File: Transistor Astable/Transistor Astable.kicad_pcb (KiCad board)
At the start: 2 copper layers, 12 parts, among them Q1 2N3904, Q2 2N3904

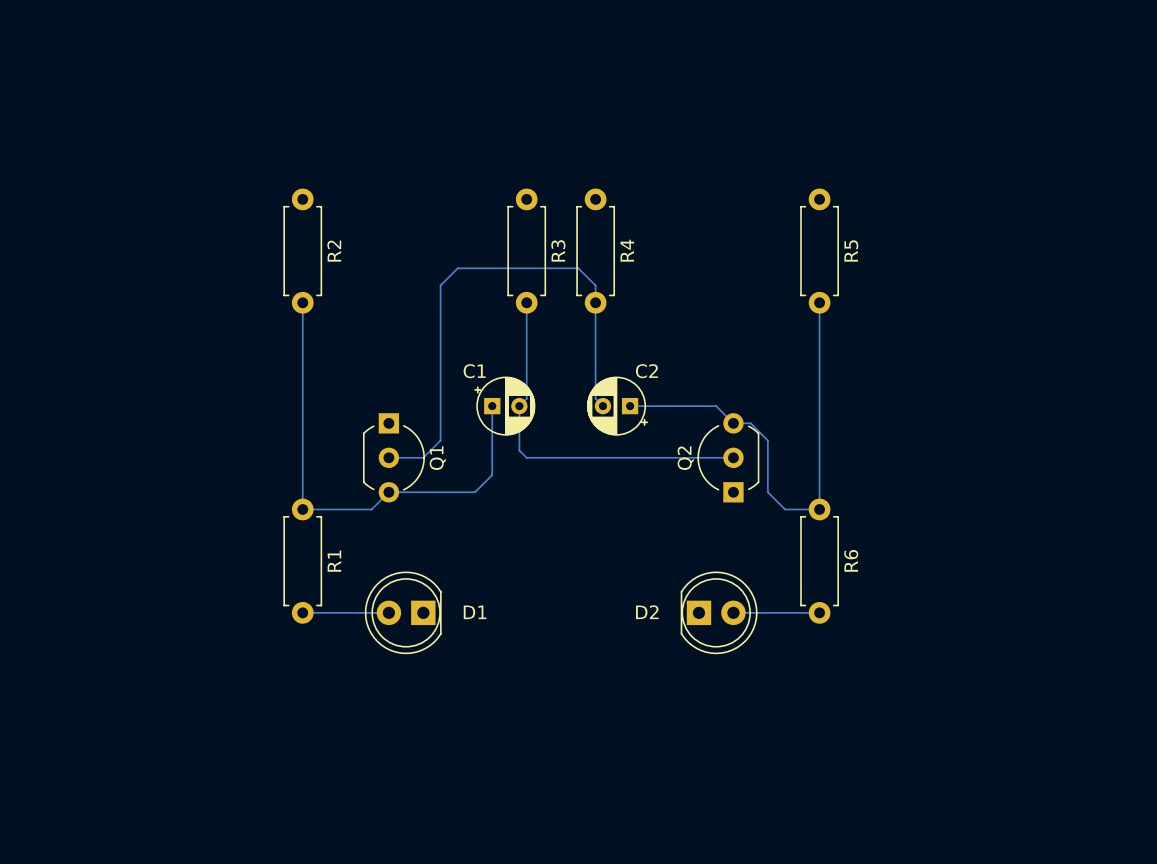
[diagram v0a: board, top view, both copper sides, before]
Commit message: Adding footprint and initial routing
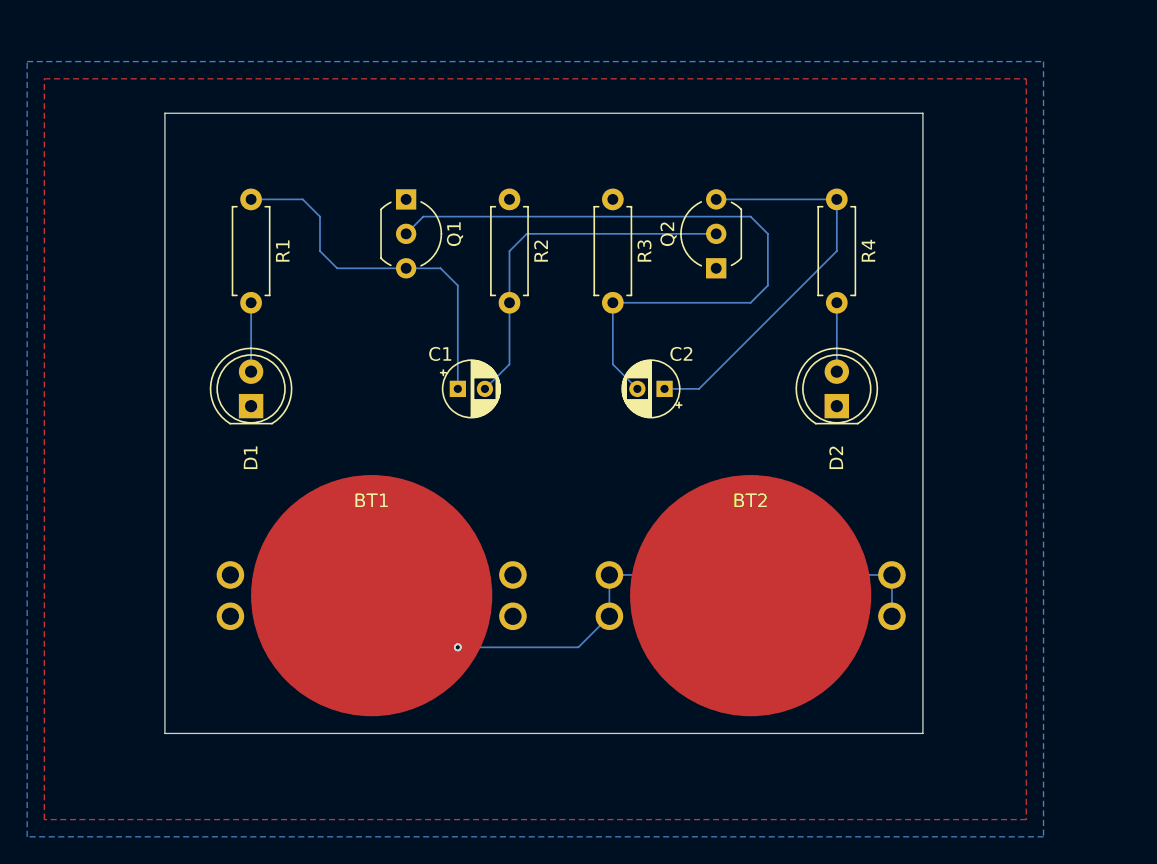
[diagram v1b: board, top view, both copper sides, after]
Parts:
- removed the R1 at (82.5, 95.2)
- removed R6: 470, Resistor_THT:R_Axial_DIN0207_L6.3mm_D2.5mm_P7.62mm_Horizontal
- added BT1: Battery_Cell, Transistor Astable:BattHold_Linx_CR2032, F.Cu at (87.6, 101.6)
- added BT2: Battery_Cell, Transistor Astable:BattHold_Linx_CR2032, F.Cu at (115.6, 101.6)
- Q1, Q2: value 2N3904 -> 2N3906
- R1: renamed from R2; value 680 -> 1k
- R4: renamed from R5; value 680 -> 1k
- moved D1 19.8 mm to (78.7, 87.6), turned to 90 degrees
- moved D2 18.3 mm to (121.9, 87.6), turned to 90 degrees
- moved Q1 16.6 mm to (90.2, 72.4)
- moved Q2 16.6 mm to (113.0, 77.5)
- moved R1 3.81 mm to (78.7, 72.4)
- moved C1 2.84 mm to (94.0, 86.4)
- moved C2 2.84 mm to (109.2, 86.4)
- moved R2 1.27 mm to (97.8, 72.4)
- moved R3 1.27 mm to (105.4, 72.4)
- moved R4 1.27 mm to (121.9, 72.4)
- renumbered R3 to R2, R4 to R3
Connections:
- Q1 pad 1: GND -> +6V
- Q2 pad 1: GND -> +6V
- R1 pad 1: +6V -> Net-(C1-Pad1)
- R1 pad 2: Net-(C1-Pad1) -> Net-(D1-Pad2)
- R2 pad 1: +6V -> GND
- R3 pad 1: +6V -> GND
- R4 pad 1: +6V -> Net-(C2-Pad1)
- R4 pad 2: Net-(C2-Pad1) -> Net-(D2-Pad2)
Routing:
- net Net-(BT1-Pad2): track 0.00 -> 39.0 mm, vias 0 -> 1
- net Net-(C2-Pad2): track 37.4 -> 50.6 mm
- net Net-(C1-Pad1): track 35.3 -> 27.0 mm
- net Net-(C2-Pad1): track 34.6 -> 29.6 mm
- net Net-(D2-Pad2): track 6.35 -> 5.08 mm
- net Net-(D1-Pad2): track 6.35 -> 5.08 mm
- added copper zone on B.Cu, net +6V
- added copper zone on F.Cu, net GND
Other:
- board outline added: 55.9 x 45.7 mm

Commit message: Routing
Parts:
- moved BT2 2.84 mm to (116.8, 104.1)
- moved BT1 2.84 mm to (86.4, 104.1)
- moved D2 2.54 mm to (124.5, 87.6)
- moved R4 2.54 mm to (124.5, 72.4)
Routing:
- net Net-(C2-Pad1): track 29.6 -> 34.7 mm
- net Net-(BT1-Pad2): track 39.0 -> 43.4 mm
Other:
- board size 55.9 x 45.7 mm -> 63.5 x 54.6 mm
- board text added: "RGE2021"
- board text added: "Transistor Astable"
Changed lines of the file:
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@@
   (general
     (thickness 1.6)
-    (drawings 4)
-    (tracks 33)
+    (drawings 10)
+    (tracks 34)
     (zones 0)
     (modules 12)
@@
   )
   (module "Transistor Astable:BattHold_Linx_CR2032" (layer F.Cu)
-    (at 115.57 101.6)
+    (at 116.84 104.14)
     (fp_text reference BT2 (at 0 -6.985) (layer F.SilkS)
       (effects (font (size 1 1) (thickness 0.15)))
@@
   )
   (module "Transistor Astable:BattHold_Linx_CR2032" (layer F.Cu)
-    (at 87.63 101.6)
+    (at 86.36 104.14)
     (fp_text reference BT1 (at 0 -6.985) (layer F.SilkS)
       (effects (font (size 1 1) (thickness 0.15)))
@@
   )
   (module Resistor_THT:R_Axial_DIN0207_L6.3mm_D2.5mm_P7.62mm_Horizontal (layer F.Cu)
-    (at 121.92 72.39 270)
+    (at 124.46 72.39 270)
     (descr "Resistor, Axial_DIN0207 series, Axial, Horizontal, pin pitch=7.62mm, 0.25W = 1/4W, length*diameter=6.3*2.5mm^2, http://cdn-reichelt.de/documents/datenblatt/B400/1_4W%23YAG.pdf")
     (tags "Resistor Axial_DIN0207 series Axial Horizontal pin pitch 7.62mm 0.25W = 1/4W length 6.3mm diameter 2.5mm")
@@
   )
   (module LED_THT:LED_D5.0mm (layer F.Cu)
-    (at 121.92 87.63 90)
+    (at 124.46 87.63 90)
     (descr "LED, diameter 5.0mm, 2 pins, http://cdn-reichelt.de/documents/datenblatt/A500/LL-504BC2E-009.pdf")
     (tags "LED diameter 5.0mm 2 pins")
@@
     )
   )
-  (gr_line (start 72.39 111.76) (end 72.39 66.04) (layer Edge.Cuts) (width 0.0381))
-  (gr_line (start 128.27 111.76) (end 72.39 111.76) (layer Edge.Cuts) (width 0.0381))
-  (gr_line (start 128.27 66.04) (end 128.27 111.76) (layer Edge.Cuts) (width 0.0381))
-  (gr_line (start 72.39 66.04) (end 128.27 66.04) (layer Edge.Cuts) (width 0.0381))
-  (via (at 93.98 105.41) (size 0.6) (drill 0.3) (layers F.Cu B.Cu) (net 9))
+  (gr_arc (start 129.54 113.03) (end 129.54 116.84) (angle -90) (layer Edge.Cuts) (width 0.0381))
+  (gr_arc (start 73.66 113.03) (end 69.85 113.03) (angle -90) (layer Edge.Cuts) (width 0.0381))
+  (gr_arc (start 129.54 66.04) (end 133.35 66.04) (angle -90) (layer Edge.Cuts) (width 0.0381))
+  (gr_arc (start 73.66 66.04) (end 73.66 62.23) (angle -90) (layer Edge.Cuts) (width 0.0381))
+  (gr_text RGE2021 (at 101.6 93.98) (layer B.Cu)
+    (effects (font (size 1.524 1.524) (thickness 0.3048)) (justify mirror))
+  )
+  (gr_text "Transistor Astable" (at 73.66 67.31) (layer F.SilkS)
+    (effects (font (size 4.064 4.064) (thickness 0.6096)) (justify left))
+  )
+  (gr_line (start 69.85 113.03) (end 69.85 66.04) (layer Edge.Cuts) (width 0.0381))
+  (gr_line (start 129.54 116.84) (end 73.66 116.84) (layer Edge.Cuts) (width 0.0381))
+  (gr_line (start 133.35 66.04) (end 133.35 113.03) (layer Edge.Cuts) (width 0.0381))
+  (gr_line (start 73.66 62.23) (end 129.54 62.23) (layer Edge.Cuts) (width 0.0381))
+  (via (at 91.44 109.22) (size 0.6) (drill 0.3) (layers F.Cu B.Cu) (net 9))
   (segment (start 95.98 86.36) (end 97.79 84.55) (width 0.127) (layer B.Cu) (net 1))
   (segment (start 97.79 84.55) (end 97.79 80.01) (width 0.127) (layer B.Cu) (net 1))
@@
   (segment (start 91.44 73.66) (end 90.17 74.93) (width 0.127) (layer B.Cu) (net 3))
   (segment (start 113.03 72.39) (end 121.92 72.39) (width 0.127) (layer B.Cu) (net 4))
-  (segment (start 111.76 86.36) (end 109.22 86.36) (width 0.127) (layer B.Cu) (net 4))
-  (segment (start 121.92 76.2) (end 111.76 86.36) (width 0.127) (layer B.Cu) (net 4))
-  (segment (start 121.92 72.39) (end 121.92 76.2) (width 0.127) (layer B.Cu) (net 4))
+  (segment (start 124.46 72.39) (end 121.92 72.39) (width 0.127) (layer B.Cu) (net 4))
+  (segment (start 109.22 86.36) (end 114.3 86.36) (width 0.127) (layer B.Cu) (net 4))
+  (segment (start 114.3 86.36) (end 124.46 76.2) (width 0.127) (layer B.Cu) (net 4))
+  (segment (start 124.46 76.2) (end 124.46 72.39) (width 0.127) (layer B.Cu) (net 4))
   (segment (start 78.74 80.01) (end 78.74 85.09) (width 0.127) (layer B.Cu) (net 5))
-  (segment (start 121.92 80.01) (end 121.92 85.09) (width 0.127) (layer B.Cu) (net 7))
-  (segment (start 93.98 105.41) (end 102.87 105.41) (width 0.127) (layer B.Cu) (net 9))
-  (segment (start 102.87 105.41) (end 105.156 103.124) (width 0.127) (layer B.Cu) (net 9))
-  (segment (start 105.156 103.124) (end 105.156 100.076) (width 0.127) (layer B.Cu) (net 9))
-  (segment (start 105.156 100.076) (end 125.984 100.076) (width 0.127) (layer B.Cu) (net 9))
-  (segment (start 125.984 100.076) (end 125.984 103.124) (width 0.127) (layer B.Cu) (net 9))
+  (segment (start 124.46 80.01) (end 124.46 85.09) (width 0.127) (layer B.Cu) (net 7))
+  (segment (start 102.87 109.22) (end 106.426 105.664) (width 0.127) (layer B.Cu) (net 9))
+  (segment (start 91.44 109.22) (end 102.87 109.22) (width 0.127) (layer B.Cu) (net 9))
+  (segment (start 106.426 105.664) (end 106.426 102.616) (width 0.127) (layer B.Cu) (net 9))
+  (segment (start 106.426 102.616) (end 127.254 102.616) (width 0.127) (layer B.Cu) (net 9))
+  (segment (start 127.254 102.616) (end 127.254 105.664) (width 0.127) (layer B.Cu) (net 9))
   (zone (net 6) (net_name GND) (layer F.Cu) (hatch edge 0.508)
     (connect_pads (clearance 0.508))
@@
     (polygon
       (pts
-        (xy 135.89 118.11) (xy 63.5 118.11) (xy 63.5 63.5) (xy 135.89 63.5)
+        (xy 135.89 118.11) (xy 63.5 118.11) (xy 63.5 60.96) (xy 135.89 60.96)
       )
     )
@@
     (polygon
       (pts
-        (xy 137.16 119.38) (xy 62.23 119.38) (xy 62.23 62.23) (xy 137.16 62.23)
+        (xy 137.16 119.38) (xy 62.23 119.38) (xy 62.23 59.69) (xy 137.16 59.69)
       )
     )
